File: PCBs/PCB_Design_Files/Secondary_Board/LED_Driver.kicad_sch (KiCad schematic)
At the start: 14 parts, among them Q1 2N3904, Q2 2N3904, Q5 2N7002, Q6 BSS84, Q7 2N7002, Q8 BSS84, U8 OPA333AIDCKR

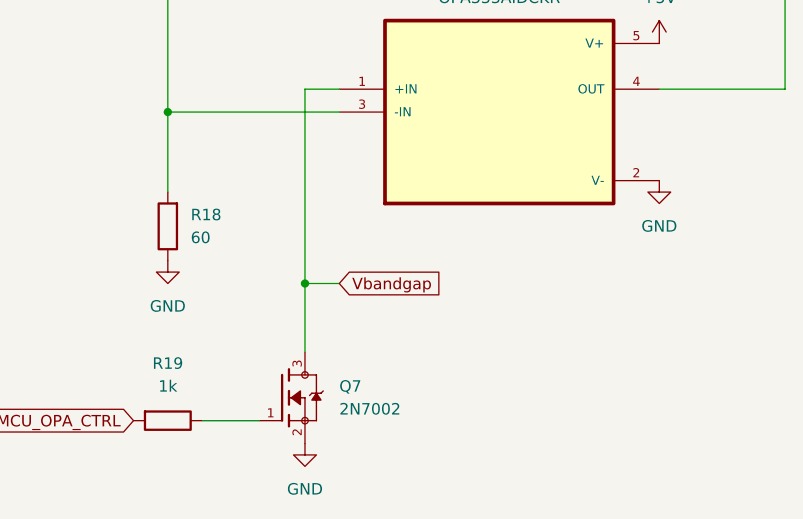
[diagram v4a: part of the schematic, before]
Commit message: LED Driver updates
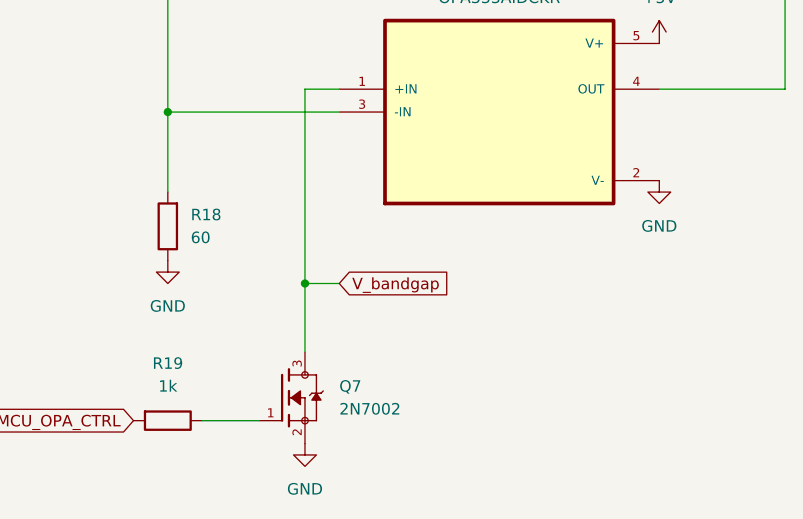
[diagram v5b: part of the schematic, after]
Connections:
- net Vbandgap renamed V_bandgap
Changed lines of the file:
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@@
 		)
 	)
-	(global_label "Vbandgap"
+	(global_label "V_bandgap"
 		(shape input)
 		(at 195.58 121.92 0)
@@
 		)
 		(property "Intersheetrefs" "${INTERSHEET_REFS}"
-			(at 207.6968 121.92 0)
+			(at 208.6644 121.92 0)
 			(effects
 				(font

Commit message: secondary board connectors
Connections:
- net MCU_IR renamed PWM_IR
- net MCU_OPA_CTRL renamed OP_CTRL
- net MCU_Red renamed PWM_Red
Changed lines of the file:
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@@
 	(paper "A4")
-	(junction
-		(at 99.06 85.09)
-		(diameter 0)
-		(color 0 0 0 0)
-	)
 	(junction
 		(at 191.77 121.92)
@@
 	)
 	(junction
-		(at 135.89 83.82)
-		(diameter 0)
-		(color 0 0 0 0)
-	)
-	(junction
 		(at 176.53 102.87)
 		(diameter 0)
@@
 	)
 	(junction
-		(at 99.06 121.92)
-		(diameter 0)
-		(color 0 0 0 0)
-	)
-	(junction
 		(at 135.89 115.57)
 		(diameter 0)
@@
 	(wire
 		(pts
-			(xy 99.06 121.92) (xy 99.06 124.46)
-		)
-		(stroke
-			(width 0)
-			(type default)
-		)
-	)
-	(wire
-		(pts
 			(xy 124.46 115.57) (xy 135.89 115.57)
 		)
@@
 	(wire
 		(pts
+			(xy 170.18 137.16) (xy 172.72 137.16)
+		)
+		(stroke
+			(width 0)
+			(type default)
+		)
+	)
+	(wire
+		(pts
 			(xy 180.34 137.16) (xy 186.69 137.16)
 		)
@@
 	(wire
 		(pts
-			(xy 135.89 92.71) (xy 135.89 83.82)
-		)
-		(stroke
-			(width 0)
-			(type default)
-		)
-	)
-	(wire
-		(pts
 			(xy 245.11 100.33) (xy 231.14 100.33)
 		)
@@
 	(wire
 		(pts
-			(xy 99.06 93.98) (xy 99.06 85.09)
+			(xy 77.47 127) (xy 80.01 127)
 		)
 		(stroke
@@
 	)
 	(label "Current Sink"
-		(at 152.4 62.23 180)
-		(effects
-			(font
-				(size 1.27 1.27)
-			)
-			(justify right bottom)
-		)
-	)
-	(label "Current Sink"
 		(at 128.27 78.74 0)
 		(effects
@@
 		)
 	)
-	(global_label "MCU_IR"
+	(hierarchical_label "V_bandgap"
 		(shape input)
-		(at 116.84 128.27 180)
-		(fields_autoplaced yes)
+		(at 195.58 121.92 0)
 		(effects
 			(font
 				(size 1.27 1.27)
 			)
-			(justify right)
-		)
-		(property "Intersheetrefs" "${INTERSHEET_REFS}"
-			(at 106.9605 128.27 0)
-			(effects
-				(font
-					(size 1.27 1.27)
-				)
-				(justify right)
-				(hide yes)
-			)
-		)
-	)
-	(global_label "MCU_Red"
+			(justify left)
+		)
+	)
+	(hierarchical_label "OP_CTRL"
 		(shape input)
-		(at 80.01 127 180)
-		(fields_autoplaced yes)
+		(at 170.18 137.16 180)
 		(effects
 			(font
@@
 			(justify right)
 		)
-		(property "Intersheetrefs" "${INTERSHEET_REFS}"
-			(at 68.4977 127 0)
-			(effects
-				(font
-					(size 1.27 1.27)
-				)
-				(justify right)
-				(hide yes)
-			)
-		)
-	)
-	(global_label "MCU_OPA_CTRL"
+	)
+	(hierarchical_label "PWM_IR"
 		(shape input)
-		(at 172.72 137.16 180)
-		(fields_autoplaced yes)
+		(at 116.84 128.27 180)
 		(effects
 			(font
@@
 			(justify right)
 		)
-		(property "Intersheetrefs" "${INTERSHEET_REFS}"
-			(at 155.5229 137.16 0)
-			(effects
-				(font
-					(size 1.27 1.27)
-				)
-				(justify right)
-				(hide yes)
-			)
-		)
-	)
-	(global_label "V_bandgap"
+	)
+	(hierarchical_label "PWM_Red"
 		(shape input)
-		(at 195.58 121.92 0)
-		(fields_autoplaced yes)
+		(at 77.47 127 180)
 		(effects
 			(font
 				(size 1.27 1.27)
 			)
-			(justify left)
-		)
-		(property "Intersheetrefs" "${INTERSHEET_REFS}"
-			(at 208.6644 121.92 0)
-			(effects
-				(font
-					(size 1.27 1.27)
-				)
-				(justify left)
-				(hide yes)
-			)
+			(justify right)
 		)
 	)
@@
 		(on_board yes)
 		(dnp no)
-		(fields_autoplaced yes)
 		(property "Reference" "Q1"
 			(at 101.6 125.7299 0)
@@
 		)
 		(property "Value" "2N3904"
-			(at 101.6 128.2699 0)
-			(effects
-				(font
+			(at 100.33 129.794 0)
+			(effects
+				(font

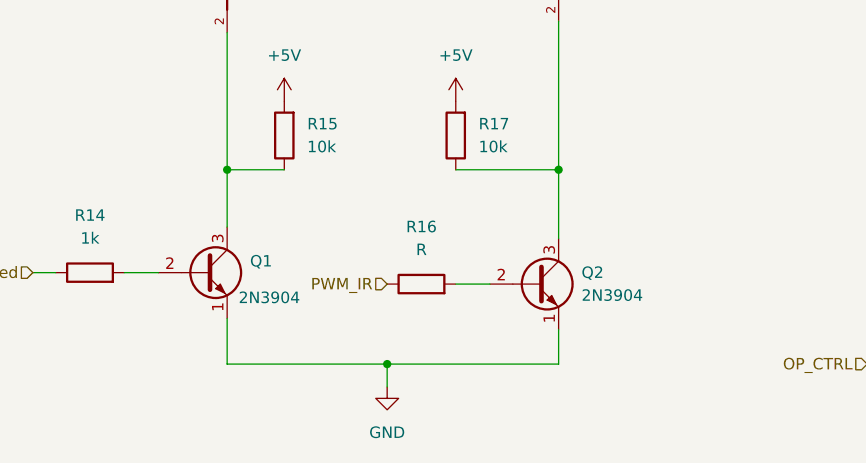
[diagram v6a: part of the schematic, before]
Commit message: LED Driver updates
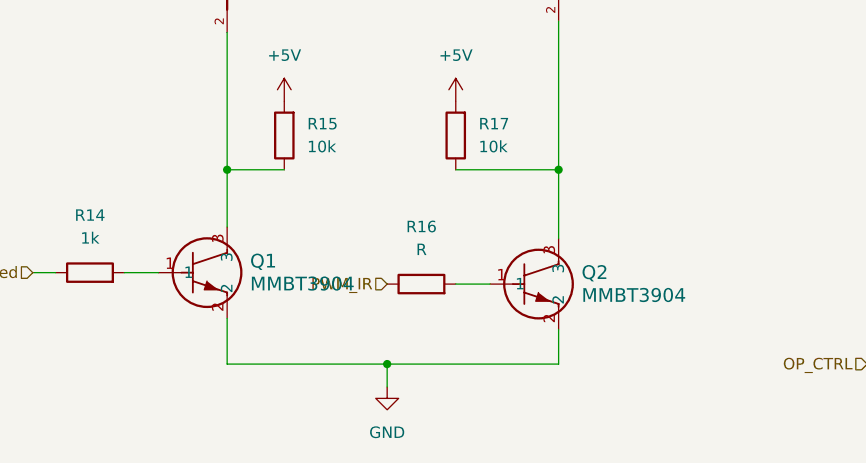
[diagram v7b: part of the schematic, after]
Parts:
- removed Q1, Q2: 2N3904, Package_TO_SOT_THT:TO-92_Inline, symbol Transistor_BJT:2N3904
- added Q1, Q2: MMBT3904, Project Footprints:SOT23_FAS, symbol Project_Symbols:MMBT3904
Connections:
- net GND: now also Q1.2, Q2.2
- net at R14.2: now also Q1.1
- net at Q6.2 (S), R15.1: now also Q1.3
- net at R16.2: now also Q2.1
- net at Q8.2 (S), R17.1: now also Q2.3

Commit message: BOM updated
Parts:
- removed Q1, Q2: MMBT3904, Project Footprints:SOT23_FAS, symbol Project_Symbols:MMBT3904
- added Q1, Q2: MMBT3904, Package_TO_SOT_SMD:SOT-23, symbol Transistor_BJT:2N3904
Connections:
- net GND: now also Q1.1 (E), Q2.1 (E)
- net at R14.2: now also Q1.2 (B)
- net at Q6.2 (S), R15.1: now also Q1.3 (C)
- net at R16.2: now also Q2.2 (B)
- net at Q8.2 (S), R17.1: now also Q2.3 (C)
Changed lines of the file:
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@@
+	)
+	(symbol
+		(lib_id "Transistor_BJT:2N3904")
+		(at 96.52 127 0)
+		(unit 1)
+		(exclude_from_sim no)
+		(in_bom yes)
+		(on_board yes)
+		(dnp no)
+		(property "Reference" "Q1"
+			(at 101.6 125.7299 0)
+			(effects
+				(font
+					(size 1.27 1.27)
+				)
+				(justify left)
+			)
+		)
+		(property "Value" "MMBT3904"
+			(at 100.33 129.794 0)
+			(effects
+				(font
+					(size 1.27 1.27)
+				)
+				(justify left)
+			)
+		)
+		(property "Footprint" "Package_TO_SOT_SMD:SOT-23"
+			(at 101.6 128.905 0)
+			(effects
+				(font
+					(size 1.27 1.27)
+					(italic yes)
+				)
+				(justify left)
+				(hide yes)
+			)
+		)
+		(property "Datasheet" "https://www.onsemi.com/pub/Collateral/2N3903-D.PDF"
+			(at 96.52 127 0)
+			(effects
+				(font
+					(size 1.27 1.27)
+				)
+				(justify left)
+				(hide yes)
+			)
+		)
+		(property "Description" "0.2A Ic, 40V Vce, Small Signal NPN Transistor, TO-92"
+			(at 96.52 127 0)
+			(effects
+				(font
+					(size 1.27 1.27)
+				)
+				(hide yes)
+			)
+		)
+		(pin "2"
+		)
+		(pin "3"
+		)
+		(pin "1"
+		)
+		(instances
+			(project "Secondary_Board"
+				(path "/2f5986e4-77b2-4f5d-ab91-80ba6228eb8b/16ecf950-1853-427b-9137-65792483b2a5"
+					(reference "Q1")
+					(unit 1)
+				)
+			)
+			(project ""
+				(path "/ed36e940-b5c2-4fa7-8175-f729e6b712de"
+					(reference "Q1")
+					(unit 1)
+				)
+			)
+		)
 	)
 	(symbol
@@
 	)
 	(symbol
-		(lib_id "Project_Symbols:MMBT3904")
-		(at 91.44 127 0)
-		(unit 1)
-		(exclude_from_sim no)
-		(in_bom yes)
-		(on_board yes)
-		(dnp no)
-		(fields_autoplaced yes)
-		(property "Reference" "Q1"
-			(at 101.6 125.7299 0)
-			(effects
-				(font
-					(size 1.524 1.524)
-				)
-				(justify left)
-			)
-		)
-		(property "Value" "MMBT3904"
-			(at 101.6 128.2699 0)
-			(effects
-				(font
-					(size 1.524 1.524)
-				)
-				(justify left)
-			)
-		)
-		(property "Footprint" "Project Footprints:SOT23_FAS"
-			(at 88.9 133.604 0)
-			(effects
-				(font
-					(size 1.27 1.27)
-					(italic yes)
-				)
-				(hide yes)
-			)
-		)
-		(property "Datasheet" "MMBT3904"
-			(at 88.9 133.604 0)
-			(effects
-				(font
-					(size 1.27 1.27)
-					(italic yes)
-				)
-				(hide yes)
-			)
-		)
-		(property "Description" ""
-			(at 91.44 127 0)
-			(effects
-				(font
-					(size 1.27 1.27)
-				)
-				(hide yes)
-			)
-		)
-		(pin "1"
-		)
-		(pin "2"
-		)
-		(pin "3"
-		)
-		(instances
-			(project ""
-				(path "/2f5986e4-77b2-4f5d-ab91-80ba6228eb8b/16ecf950-1853-427b-9137-65792483b2a5"
-					(reference "Q1")
-					(unit 1)
-				)
-			)
-		)
-	)
-	(symbol
 		(lib_id "Device:R")
 		(at 120.65 128.27 90)
@@
 	)
 	(symbol
+		(lib_id "Transistor_BJT:2N3904")
+		(at 133.35 128.27 0)
+		(unit 1)
+		(exclude_from_sim no)
+		(in_bom yes)
+		(on_board yes)
+		(dnp no)
+		(fields_autoplaced yes)
+		(property "Reference" "Q2"
+			(at 138.43 126.9999 0)
+			(effects
+				(font
+					(size 1.27 1.27)
+				)
+				(justify left)
+			)
+		)
+		(property "Value" "MMBT3904"
+			(at 138.43 129.5399 0)
+			(effects
+				(font
+					(size 1.27 1.27)
+				)
+				(justify left)
+			)
+		)
+		(property "Footprint" "Package_TO_SOT_SMD:SOT-23"
+			(at 138.43 130.175 0)
+			(effects
+				(font
+					(size 1.27 1.27)
+					(italic yes)
+				)
+				(justify left)
+				(hide yes)
+			)
+		)
+		(property "Datasheet" "https://www.onsemi.com/pub/Collateral/2N3903-D.PDF"
+			(at 133.35 128.27 0)
+			(effects
+				(font
+					(size 1.27 1.27)
+				)
+				(justify left)
+				(hide yes)
+			)
+		)
+		(property "Description" "0.2A Ic, 40V Vce, Small Signal NPN Transistor, TO-92"
+			(at 133.35 128.27 0)
+			(effects
+				(font
+					(size 1.27 1.27)
+				)
+				(hide yes)
+			)
+		)
+		(pin "3"
+		)
+		(pin "2"
+		)
+		(pin "1"
+		)
+		(instances
+			(project "Secondary_Board"
+				(path "/2f5986e4-77b2-4f5d-ab91-80ba6228eb8b/16ecf950-1853-427b-9137-65792483b2a5"
+					(reference "Q2")
+					(unit 1)
+				)
+			)
+			(project ""
+				(path "/ed36e940-b5c2-4fa7-8175-f729e6b712de"
+					(reference "Q2")
+					(unit 1)
+				)
+			)
+		)
+	)
+	(symbol
 		(lib_id "Project_Symbols:2N7002")
 		(at 179.07 74.93 0)
@@
 					(unit 1)
 				)
-			)
-		)
-	)
-	(symbol
-		(lib_id "Project_Symbols:MMBT3904")
-		(at 128.27 128.27 0)
-		(unit 1)
-		(exclude_from_sim no)
-		(in_bom yes)
-		(on_board yes)
-		(dnp no)
-		(fields_autoplaced yes)
-		(property "Reference" "Q2"
-			(at 138.43 126.9999 0)
-			(effects
-				(font
-					(size 1.524 1.524)
-				)
-				(justify left)
-			)
-		)
-		(property "Value" "MMBT3904"
-			(at 138.43 129.5399 0)
-			(effects
-				(font
-					(size 1.524 1.524)
-				)
-				(justify left)
-			)
-		)
-		(property "Footprint" "Project Footprints:SOT23_FAS"
-			(at 125.73 134.874 0)
-			(effects
-				(font
-					(size 1.27 1.27)
-					(italic yes)
-				)
-				(hide yes)
-			)
-		)
-		(property "Datasheet" "MMBT3904"
-			(at 125.73 134.874 0)
-			(effects
-				(font
-					(size 1.27 1.27)
-					(italic yes)
-				)
-				(hide yes)
-			)
-		)
-		(property "Description" ""
-			(at 128.27 128.27 0)
-			(effects
-				(font
-					(size 1.27 1.27)
-				)
-				(hide yes)
-			)
-		)
-		(pin "1"
-		)
-		(pin "3"
-		)
-		(pin "2"
-		)
-		(instances
-			(project ""
-				(path "/2f5986e4-77b2-4f5d-ab91-80ba6228eb8b/16ecf950-1853-427b-9137-65792483b2a5"
-					(reference "Q2")
-					(unit 1)
-				)
